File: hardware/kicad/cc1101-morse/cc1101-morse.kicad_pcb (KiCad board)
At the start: 2 copper layers, 40 x 60 mm, 7 parts, among them J1 Conn_02x04_Odd_Even, SW1 SW_Push, U1 ESP32-C3-SuperMini

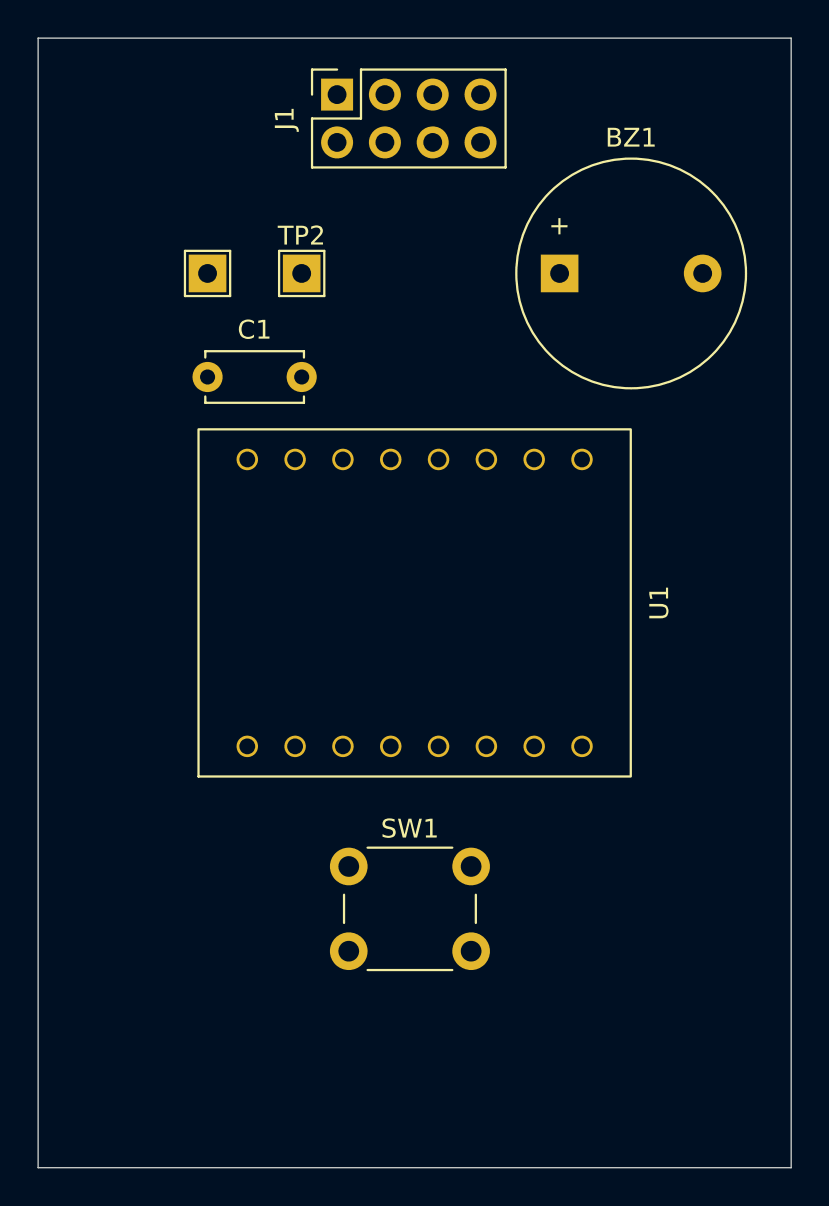
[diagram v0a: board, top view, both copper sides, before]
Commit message: Reassign SPI pins so the traces stop crossing
The first autoroute stalled with a net it could not finish. The cause
was not the router: the straight-line paths between J1 and U1 crossed
each other five times among seven nets, because the connector's
left-hand pins were assigned to the MCU's right-hand pins and back
again. On a two-layer board a crossing is a via; on one layer it is a
trace that cannot be routed at all.

Every SPI line here is bit-banged, so the mapping is free. Searched
for the permutation with no crossings instead of guessing:

  MOSI  GPIO2 -> GPIO6
  SCK   GPIO3 -> GPIO5
  MISO  GPIO4 -> GPIO2

Zero crossings. The search was restricted to GPIO0-7 on purpose —
allowing GPIO8/9/21 found a route 41 mm shorter, but those are the
strapping pins and I2C defaults that decisions.md §7 reserves for an
OLED, and the shorter route was not worth spending them.

Costs the CC1101 pins matching Sparks, which only affects radio.cpp —
a file Sparks does not have. key.cpp and sidetone.cpp still share
GPIO10 and GPIO20 with it.
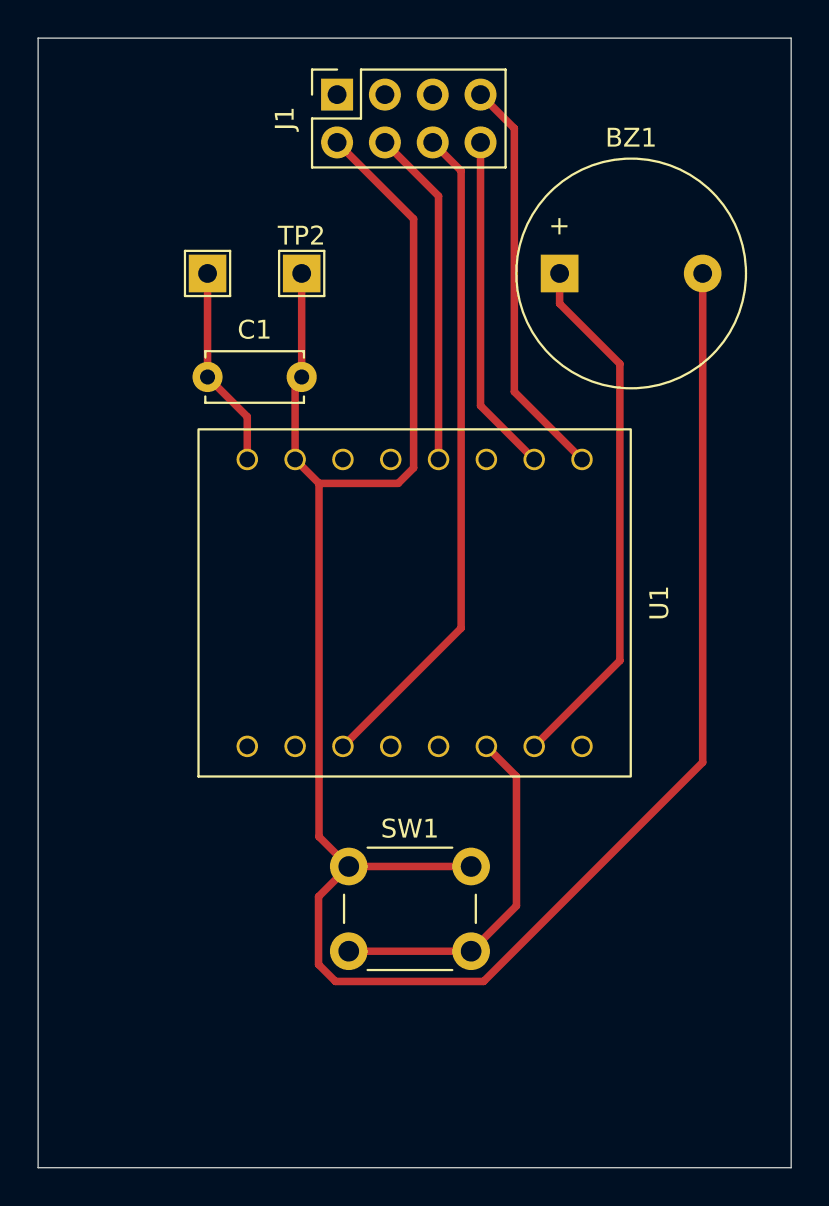
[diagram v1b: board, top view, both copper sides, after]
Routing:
- net GND: track 0.00 -> 121.1 mm
- net Net-(J1-Pin_6): track 0.00 -> 35.3 mm
- net Net-(BZ1-+): track 0.00 -> 28.3 mm
- net Net-(J1-Pin_7): track 0.00 -> 21.6 mm
- net Net-(U1-GPIO10): track 0.00 -> 19.0 mm
- net Net-(J1-Pin_4): track 0.00 -> 18.0 mm
- net Net-(J1-Pin_8): track 0.00 -> 18.0 mm
- net +5V: track 0.00 -> 10.8 mm

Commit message: Board: GND pour, mounting holes, J1 rewired to new pins
The schematic now matches the reassigned SPI pins (MOSI GPIO6, SCK
GPIO5, MISO GPIO2) — verified against the netlist, all eight J1 pins
correct.

Ground is a filled zone on F.Cu rather than the perimeter trace
decisions.md §3 specified. The pour is the better choice here and the
earlier objection to it was wrong: the board is 40x60 mm with 17
thin traces, so there is no fragmentation risk, and the connection
the autorouter could not make (BZ1.2 -> J1.2) is solved for free by
both pads dropping into the fill. It also suits the process — a fiber
laser removes copper, so leaving a pour is less etching, not more.

Four mounting holes added, one per corner, inset ~3 mm.
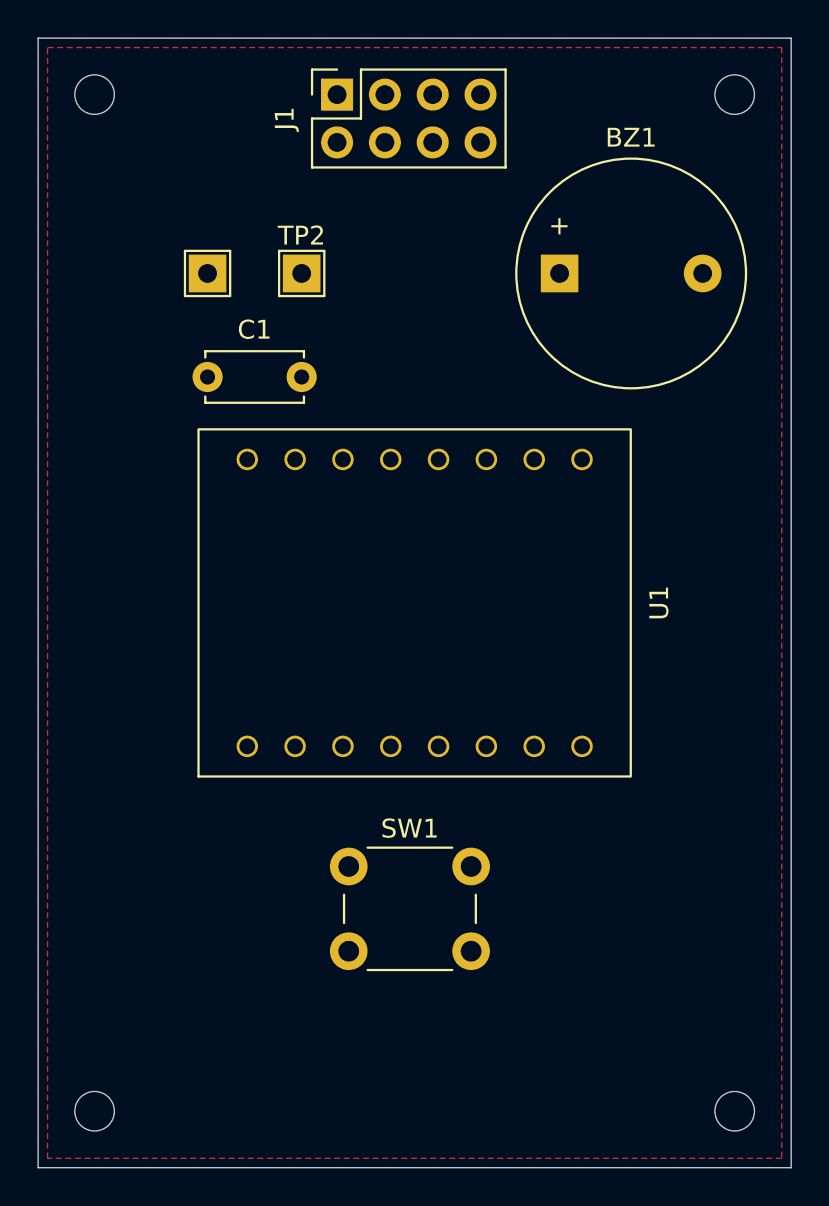
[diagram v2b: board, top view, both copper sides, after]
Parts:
- added REF**: MountingHole_2.1mm, MountingHole:MountingHole_2.1mm, F.Cu at (133.0, 127.5)
- added REF**: MountingHole_2.1mm, MountingHole:MountingHole_2.1mm, F.Cu at (167.0, 127.5)
- added REF**: MountingHole_2.1mm, MountingHole:MountingHole_2.1mm, F.Cu at (133.0, 73.5)
- added REF**: MountingHole_2.1mm, MountingHole:MountingHole_2.1mm, F.Cu at (167.0, 73.5)
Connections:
- U1 pad 10: unconnected-(U1-GPIO6-Pad10) -> Net-(J1-Pin_3)
- U1 pad 3: Net-(J1-Pin_3) -> Net-(J1-Pin_5)
- U1 pad 4: Net-(J1-Pin_4) -> unconnected-(U1-GPIO3-Pad4)
- U1 pad 5: Net-(J1-Pin_5) -> unconnected-(U1-GPIO4-Pad5)
- U1 pad 9: unconnected-(U1-GPIO5-Pad9) -> Net-(J1-Pin_4)
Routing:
- net GND: track 121.1 -> 1.17 mm
- net Net-(J1-Pin_6): track 35.3 -> 0.00 mm
- net Net-(BZ1-+): track 28.3 -> 0.00 mm
- net Net-(J1-Pin_7): track 21.6 -> 0.00 mm
- net Net-(U1-GPIO10): track 19.0 -> 0.00 mm
- net Net-(J1-Pin_4): track 18.0 -> 0.00 mm
- net Net-(J1-Pin_8): track 18.0 -> 0.00 mm
- net +5V: track 10.8 -> 0.00 mm
- added copper zone on F.Cu, net GND

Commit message: Annotate mounting holes H1-H4
All four shared the placeholder REF**, which blocked Specctra DSN
export ("Multiple footprints have the reference designator REF**").
Numbered by position, top row first, left to right.
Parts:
- renumbered REF** to H1, REF** to H2, REF** to H3, REF** to H4
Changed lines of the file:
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@@
 		(descr "Mounting Hole 2.1mm, no annular, generated by kicad-footprint-generator mountinghole.py")
 		(tags "mountinghole")
-		(property "Reference" "REF**"
+		(property "Reference" "H3"
 			(at 0 -3.05 0)
 			(layer "F.SilkS")
@@
 			(fill no)
 			(layer "F.CrtYd")
-		)
-		(fp_text user "${REFERENCE}"
-			(at 0 0 0)
-			(layer "F.Fab")
-			(effects
-				(font
-					(size 1 1)
-					(thickness 0.15)
-				)
-			)
 		)
 		(pad "" np_thru_hole circle
@@
 		(descr "Mounting Hole 2.1mm, no annular, generated by kicad-footprint-generator mountinghole.py")
 		(tags "mountinghole")
-		(property "Reference" "REF**"
+		(property "Reference" "H4"
 			(at 0 -3.05 0)
 			(layer "F.SilkS")
@@
 			(fill no)
 			(layer "F.CrtYd")
-		)
-		(fp_text user "${REFERENCE}"
-			(at 0 0 0)
-			(layer "F.Fab")
-			(effects
-				(font
-					(size 1 1)
-					(thickness 0.15)
-				)
-			)
 		)
 		(pad "" np_thru_hole circle
@@
 		(descr "Mounting Hole 2.1mm, no annular, generated by kicad-footprint-generator mountinghole.py")
 		(tags "mountinghole")
-		(property "Reference" "REF**"
+		(property "Reference" "H1"
 			(at 0 -3.05 0)
 			(layer "F.SilkS")
@@
 			(fill no)
 			(layer "F.CrtYd")
-		)
-		(fp_text user "${REFERENCE}"
-			(at 0 0 0)
-			(layer "F.Fab")
-			(effects
-				(font
-					(size 1 1)
-					(thickness 0.15)
-				)
-			)
 		)
 		(pad "" np_thru_hole circle
@@
 		(descr "Mounting Hole 2.1mm, no annular, generated by kicad-footprint-generator mountinghole.py")
 		(tags "mountinghole")
-		(property "Reference" "REF**"
+		(property "Reference" "H2"
 			(at 0 -3.05 0)
 			(layer "F.SilkS")
@@
 			(layer "F.CrtYd")
 		)
-		(fp_text user "${REFERENCE}"
-			(at 0 0 0)
-			(layer "F.Fab")
-			(effects
-				(font
-					(size 1 1)
-					(thickness 0.15)
-				)
-			)
-		)
 		(pad "" np_thru_hole circle

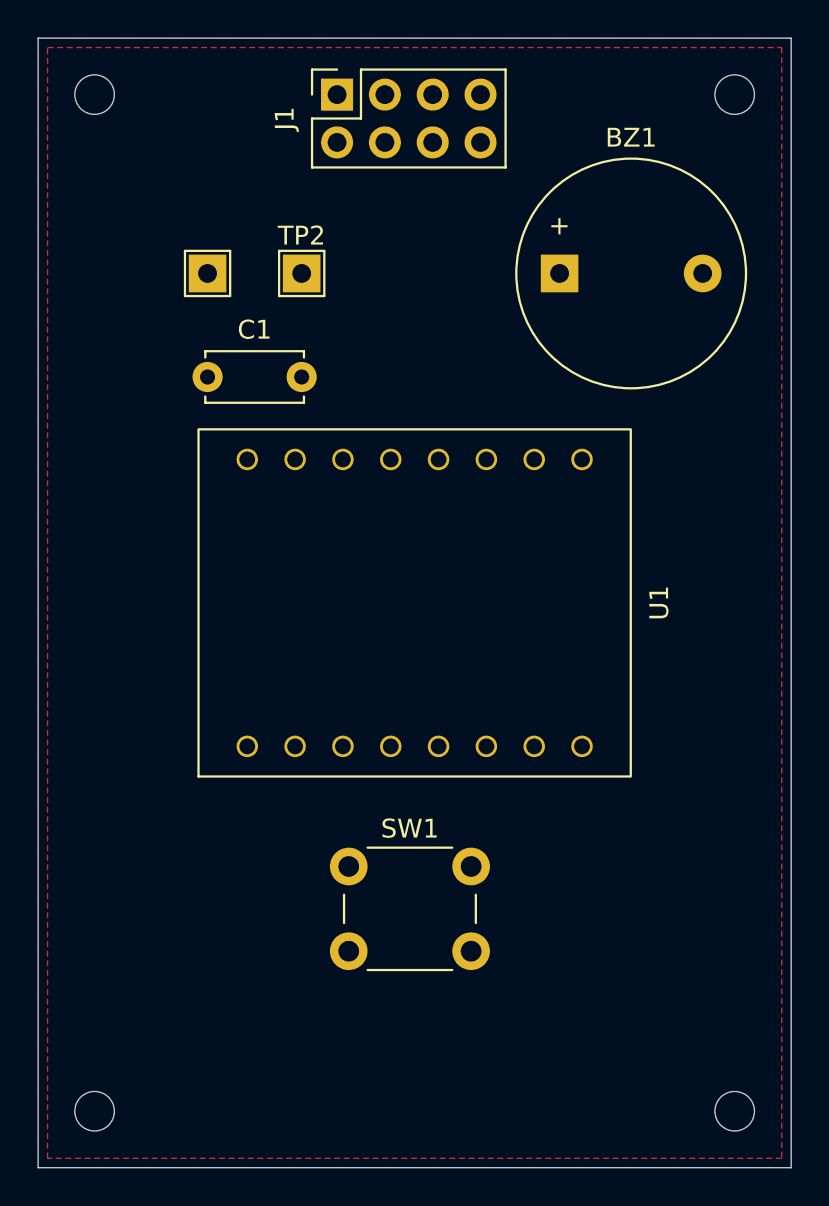
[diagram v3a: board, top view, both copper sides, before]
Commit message: Rewrite docs to stand on their own
The docs were framed throughout as a comparison against another
board — decisions explained as "that project did X, here is why this
one does not". Every decision now argues from its own merits instead.

decisions.md is the main rewrite. §1 is no longer "no LED panel" but
"no display", and explains the cost directly: a panel needs a driver
IC, most are 5 V parts, 5 V needs level shifting and a boost
converter, and the driver's addressing rarely matches the physical
layout, which forces a second layer. The point is the chain, not that
some other board went down it.

Also adds §10 for the ground pour, which was decided in practice but
never written down, and folds the perimeter-trace plan it replaced
into the same entry.

Drops the BOM's "not on this board" table — it was a list of parts
another board has.
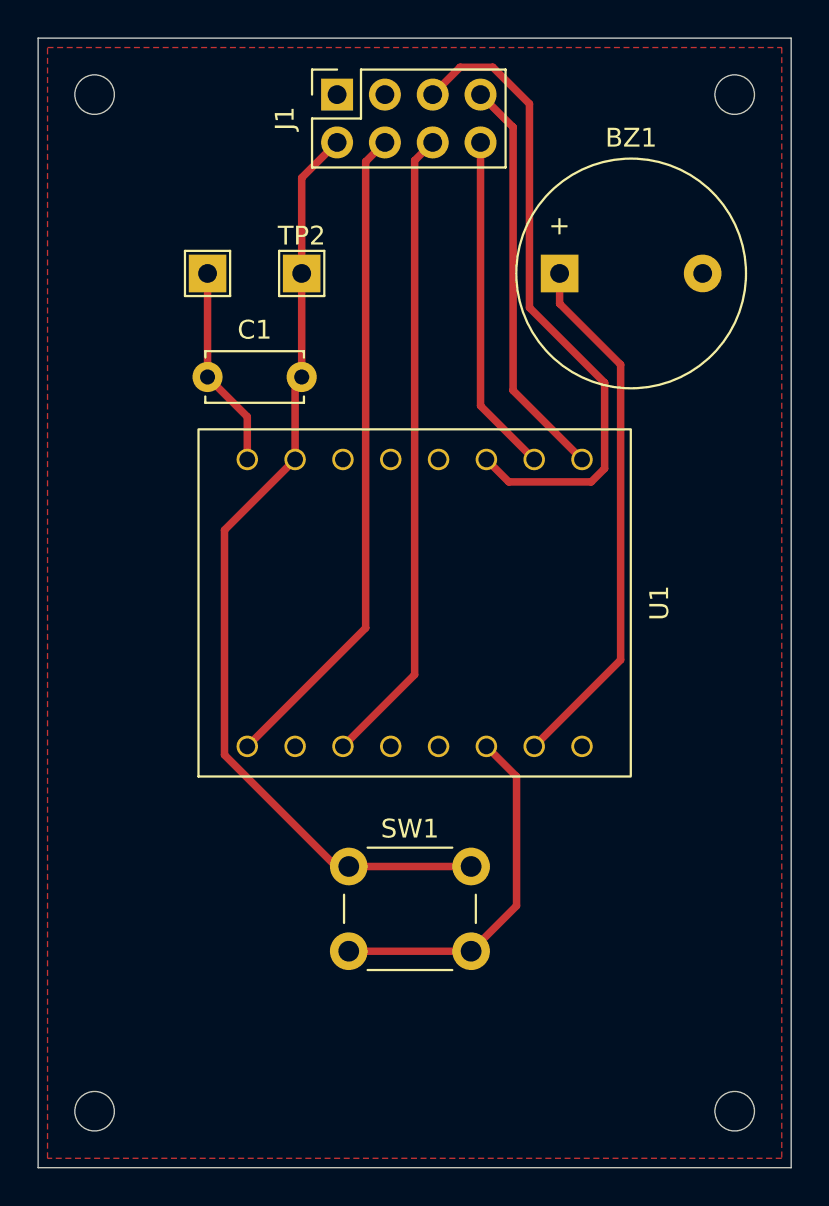
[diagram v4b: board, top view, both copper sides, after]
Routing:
- net GND: track 1.17 -> 50.6 mm
- net Net-(J1-Pin_4): track 0.00 -> 35.1 mm
- net Net-(J1-Pin_5): track 0.00 -> 34.6 mm
- net Net-(J1-Pin_6): track 0.00 -> 34.1 mm
- net Net-(BZ1-+): track 0.00 -> 28.4 mm
- net Net-(J1-Pin_7): track 0.00 -> 21.6 mm
- net Net-(U1-GPIO10): track 0.00 -> 19.0 mm
- net Net-(J1-Pin_8): track 0.00 -> 18.0 mm
- net +5V: track 0.00 -> 10.8 mm

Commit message: Route the board by hand: DRC clean
54 segments on F.Cu, no vias, ground poured. DRC reports 0 violations,
0 unconnected, 0 schematic parity errors.

Routed by hand after three autoroute attempts failed to produce a
usable board. Freerouting could not see the mounting holes (it logged
"could not read keepout area" on every run) and had no way to know
that J1's GND pad needs a clear corridor for the pour to reach it —
which is what left it isolated each time. Nine nets over ~227 mm was
always inside hand-routing distance.
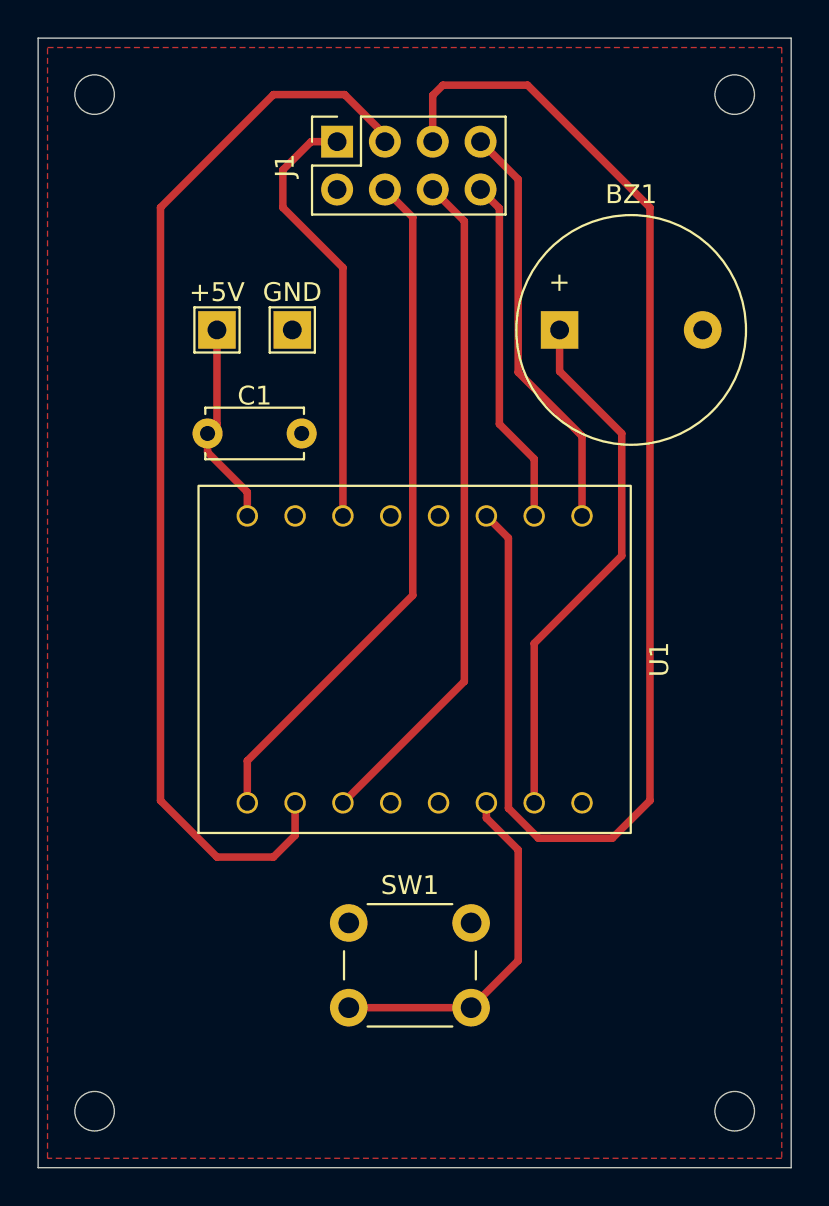
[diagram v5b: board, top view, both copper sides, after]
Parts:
- moved TP1 3.04 mm to (139.5, 86.0)
- moved TP2 3.04 mm to (143.5, 86.0)
- moved BZ1 3.00 mm to (157.7, 86.0)
- moved C1 3.00 mm to (139.0, 91.5)
- moved SW1 3.00 mm to (146.5, 117.5)
- moved U1 3.00 mm to (150.0, 103.5)
- moved J1 2.50 mm to (145.9, 76.0)
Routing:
- net Net-(J1-Pin_3): track 0.00 -> 57.8 mm
- net GND: track 50.6 -> 0.00 mm
- net Net-(J1-Pin_5): track 34.6 -> 73.4 mm
- net Net-(J1-Pin_1): track 0.00 -> 23.2 mm
- net Net-(J1-Pin_6): track 34.1 -> 35.9 mm
- net Net-(J1-Pin_4): track 35.1 -> 36.8 mm
- net Net-(J1-Pin_8): track 18.0 -> 18.5 mm

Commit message: Add C2, decoupling the CC1101's own 3V3 rail
C1 sits across +5V near the Supermini — input decoupling for the
regulator, which is a real job but not the radio's. The CC1101 runs
from +3V3 and had no local capacitor at all.

C2 fills that gap. In TX the radio switches ~35 mA on and off at
keying speed while SPI is bit-banged alongside it, so every mark is a
step change in current. The regulator answers in microseconds and the
trace to the socket has inductance; C2 supplies that first instant
locally.

Likely unnecessary at these currents, but the failure mode if it is
needed and missing — intermittent SPI errors, or the radio dropping
out only while transmitting — is much worse to diagnose than one
through-hole part is to fit.

Docs corrected throughout: the BOM described C1 as "CC1101 supply
decoupling, place close to the socket's VCC pin", which was the job
C2 now does.

DRC clean: 0 violations, 0 unconnected, 0 parity.
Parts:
- added C2: 100n, Capacitor_THT:C_Disc_D5.0mm_W2.5mm_P5.00mm, F.Cu at (146.0, 92.0)
- C1: value C -> 100n
- moved TP2 7.16 mm to (137.0, 83.0)
- moved TP1 3.35 mm to (141.0, 83.0)
- moved C1 2.06 mm to (141.0, 92.0), turned to 90 degrees
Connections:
- net Net-(J1-Pin_1) renamed +3V3
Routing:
- net +5V: track 11.0 -> 14.6 mm
- net Net-(J1-Pin_3): track 57.8 -> 60.3 mm
